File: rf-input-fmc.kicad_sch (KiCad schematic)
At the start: 0 parts

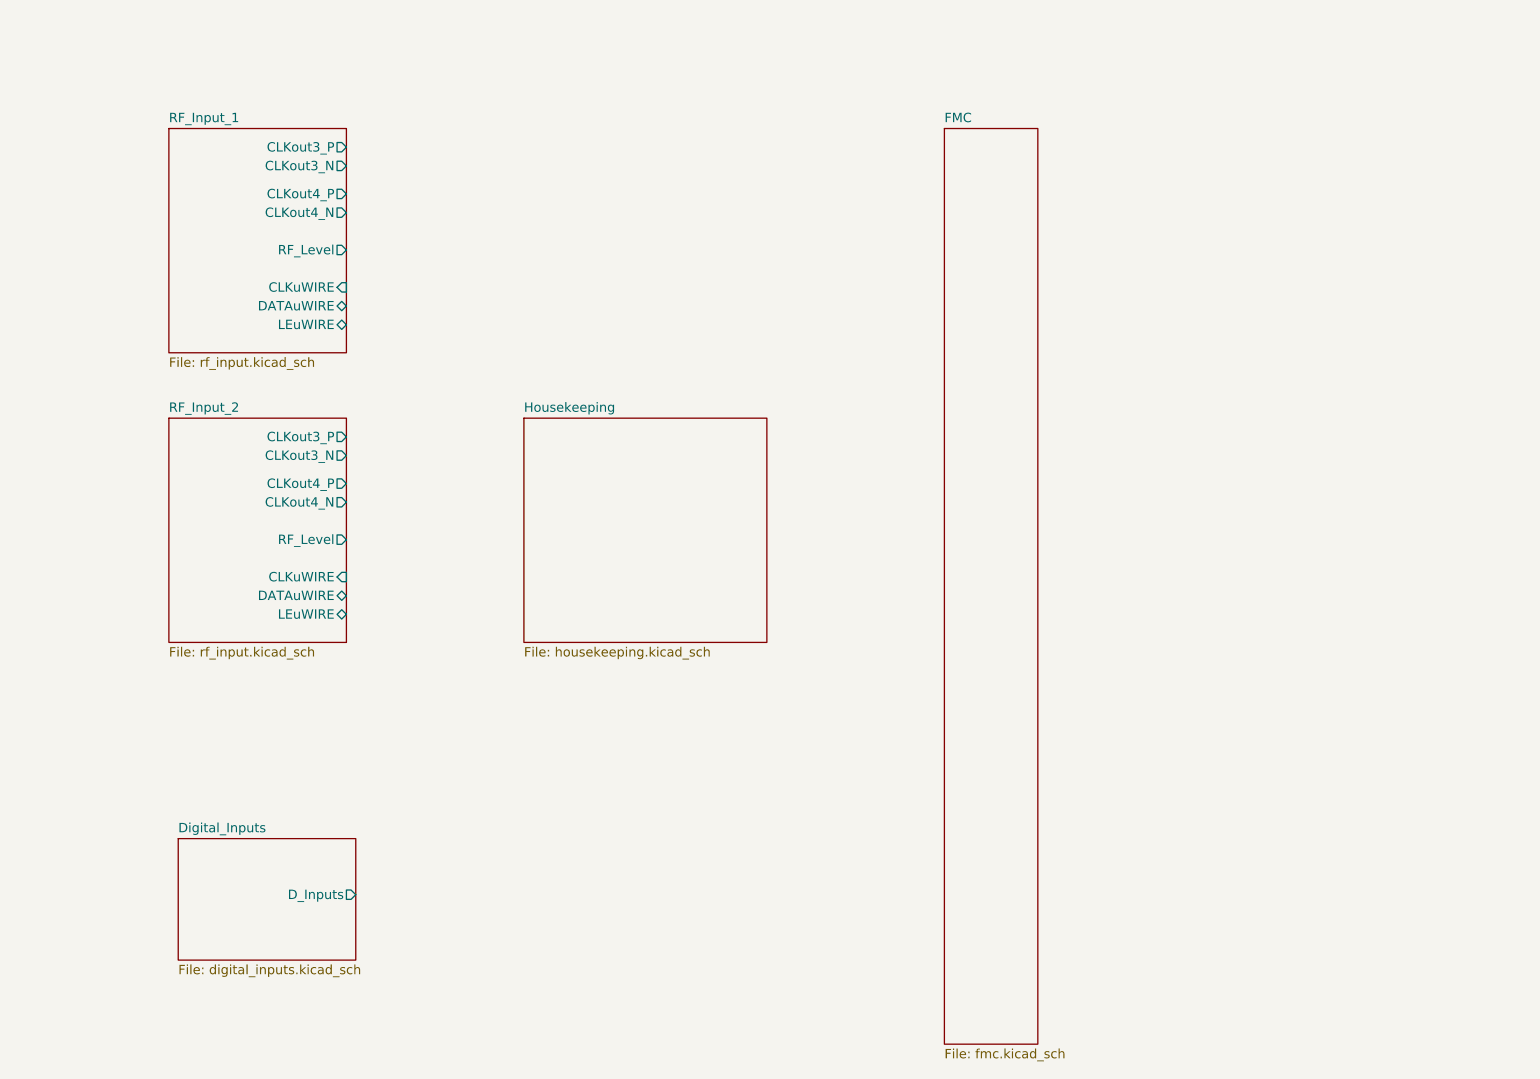
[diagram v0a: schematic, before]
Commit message: Draft Schematic Complete
-See design.md for remaining design work/questions
-See output folder for current schematic prints
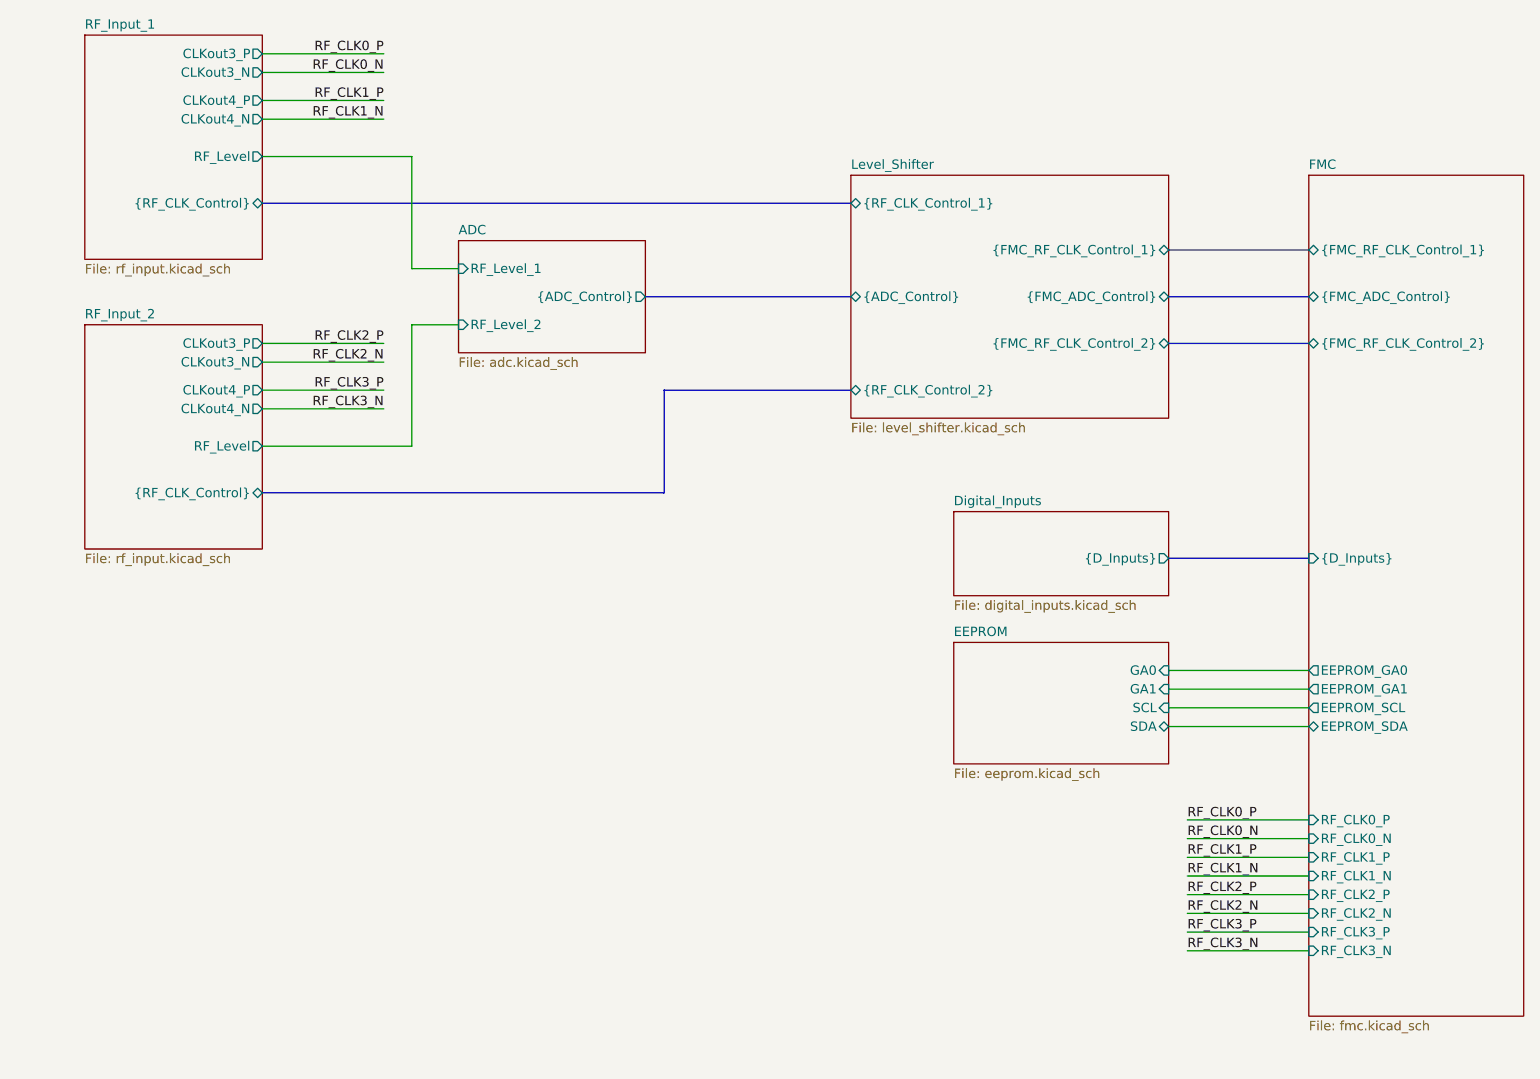
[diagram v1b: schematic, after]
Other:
- sheet Housekeeping renamed Level_Shifter
- added sheet ADC (adc.kicad_sch)
- added sheet EEPROM (eeprom.kicad_sch)
- sheet Digital_Inputs ports: added {D_Inputs}; removed D_Inputs
- sheet FMC ports: added EEPROM_GA0, EEPROM_GA1, EEPROM_SCL, EEPROM_SDA, RF_CLK0_N, RF_CLK0_P, RF_CLK1_N, RF_CLK1_P, RF_CLK2_N, RF_CLK2_P, RF_CLK3_N, RF_CLK3_P, {D_Inputs}, {FMC_ADC_Control}, {FMC_RF_CLK_Control_1}, {FMC_RF_CLK_Control_2}; removed none
- sheet Level_Shifter: file housekeeping.kicad_sch -> level_shifter.kicad_sch
- sheet Level_Shifter ports: added {ADC_Control}, {FMC_ADC_Control}, {FMC_RF_CLK_Control_1}, {FMC_RF_CLK_Control_2}, {RF_CLK_Control_1}, {RF_CLK_Control_2}; removed none
- sheet RF_Input_1 ports: added {RF_CLK_Control}; removed CLKuWIRE, DATAuWIRE, LEuWIRE
- sheet RF_Input_2 ports: added {RF_CLK_Control}; removed CLKuWIRE, DATAuWIRE, LEuWIRE
- company: (none) -> Osprey DCS
- title: (none) -> RF Input FMC Board

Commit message: fixup some hierarchical buses
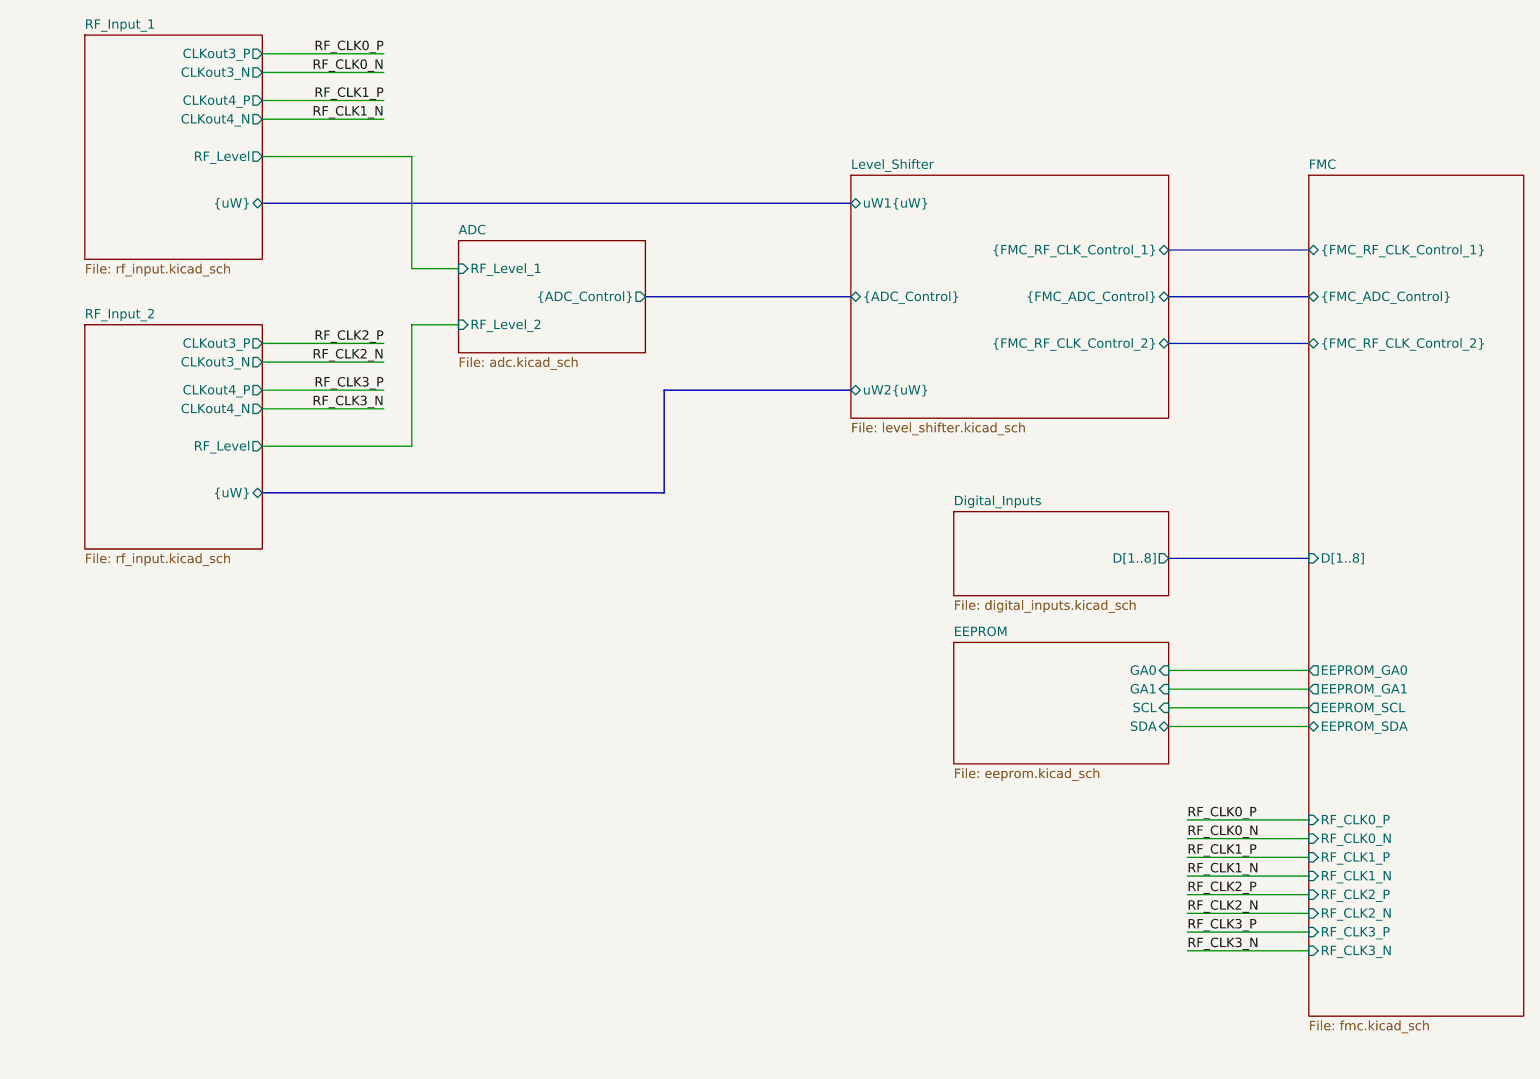
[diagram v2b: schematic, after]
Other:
- sheet Digital_Inputs ports: added D[1..8]; removed {D_Inputs}
- sheet FMC ports: added D[1..8]; removed {D_Inputs}
- sheet Level_Shifter ports: added uW1{uW}, uW2{uW}; removed {RF_CLK_Control_1}, {RF_CLK_Control_2}
- sheet RF_Input_1 ports: added {uW}; removed {RF_CLK_Control}
- sheet RF_Input_2 ports: added {uW}; removed {RF_CLK_Control}
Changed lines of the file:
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@@
 			)
 		)
-		(pin "{RF_CLK_Control}" bidirectional
+		(pin "{uW}" bidirectional
 			(at 69.85 86.36 0)
 			(effects
@@
 			)
 		)
-		(pin "{D_Inputs}" output
+		(pin "D[1..8]" output
 			(at 193.04 95.25 0)
 			(effects
@@
 			)
 		)
-		(pin "{RF_CLK_Control}" bidirectional
+		(pin "{uW}" bidirectional
 			(at 69.85 46.99 0)
 			(effects
@@
 			)
 		)
-		(pin "{RF_CLK_Control_1}" bidirectional
+		(pin "uW1{uW}" bidirectional
 			(at 149.86 46.99 180)
 			(effects
@@
 			)
 		)
-		(pin "{RF_CLK_Control_2}" bidirectional
+		(pin "uW2{uW}" bidirectional
 			(at 149.86 72.39 180)
 			(effects
@@
 			)
 		)
-		(pin "{D_Inputs}" input
+		(pin "D[1..8]" input
 			(at 212.09 95.25 180)
 			(effects

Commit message: Schamtic Revision
- Added 8 more D inputs
- Removed 1 LMK01801 IC
- Cleaned up some buses
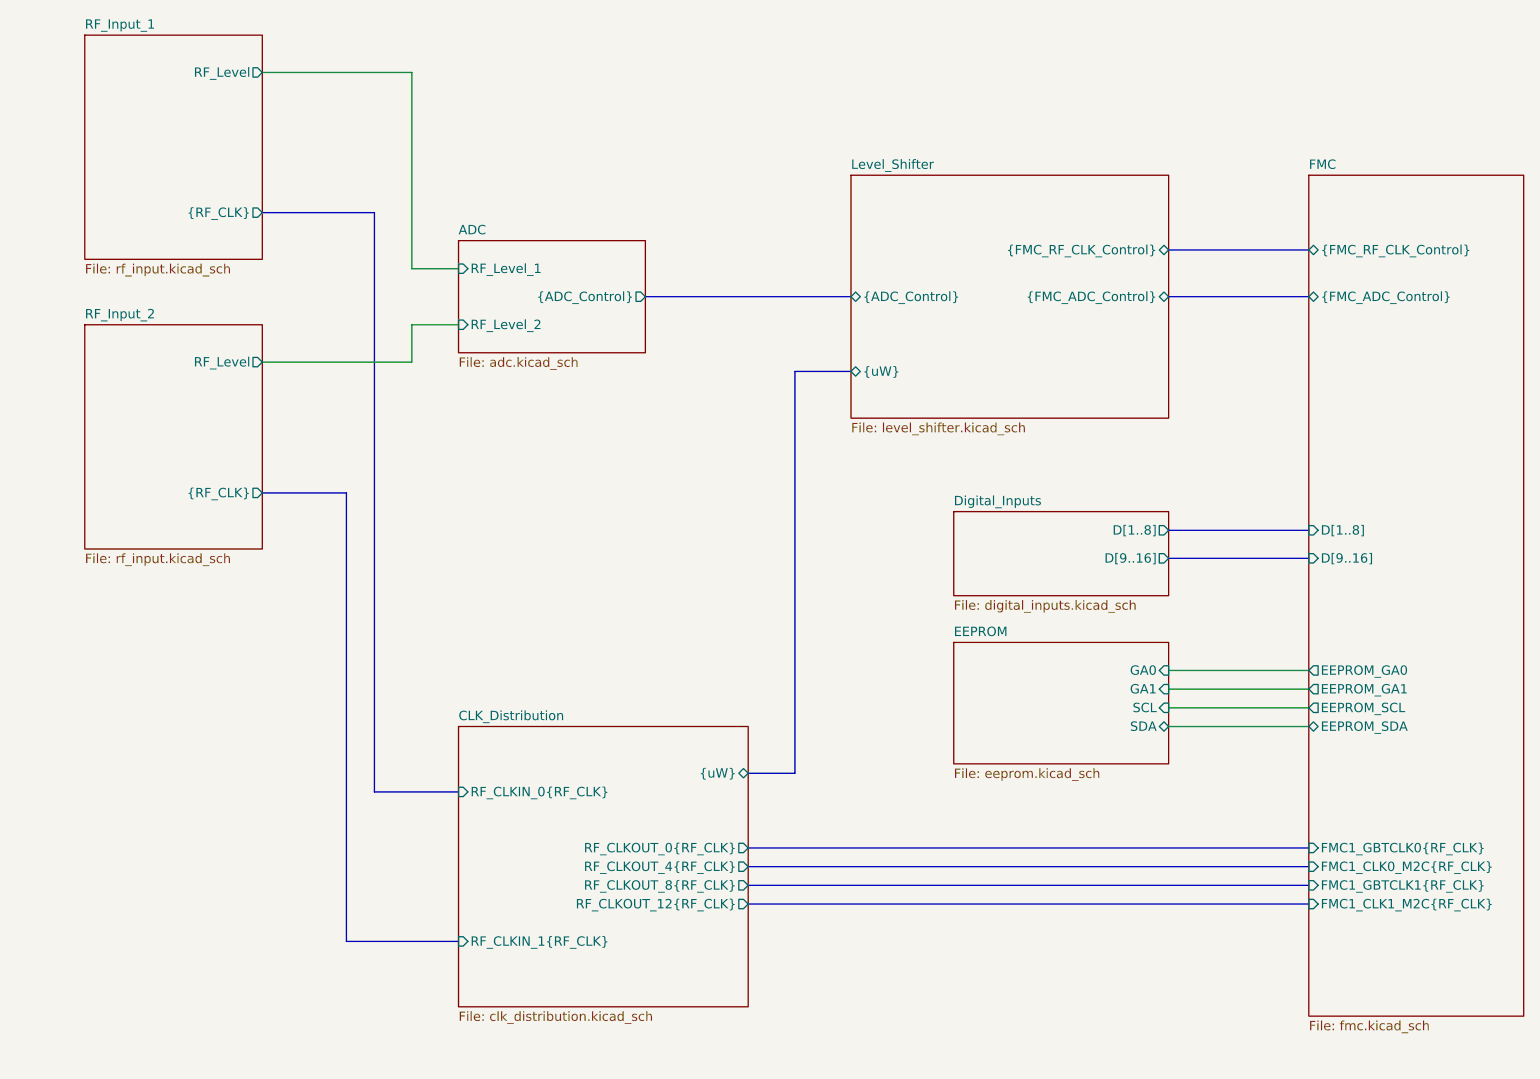
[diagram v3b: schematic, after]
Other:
- added sheet CLK_Distribution (clk_distribution.kicad_sch)
- sheet Digital_Inputs ports: added D[9..16]; removed none
- sheet FMC ports: added D[9..16], FMC1_CLK0_M2C{RF_CLK}, FMC1_CLK1_M2C{RF_CLK}, FMC1_GBTCLK0{RF_CLK}, FMC1_GBTCLK1{RF_CLK}, {FMC_RF_CLK_Control}; removed RF_CLK0_N, RF_CLK0_P, RF_CLK1_N, RF_CLK1_P, RF_CLK2_N, RF_CLK2_P, RF_CLK3_N, RF_CLK3_P, {FMC_RF_CLK_Control_1}, {FMC_RF_CLK_Control_2}
- sheet Level_Shifter ports: added {FMC_RF_CLK_Control}, {uW}; removed uW1{uW}, uW2{uW}, {FMC_RF_CLK_Control_1}, {FMC_RF_CLK_Control_2}
- sheet RF_Input_1 ports: added {RF_CLK}; removed CLKout3_N, CLKout3_P, CLKout4_N, CLKout4_P, {uW}
- sheet RF_Input_2 ports: added {RF_CLK}; removed CLKout3_N, CLKout3_P, CLKout4_N, CLKout4_P, {uW}

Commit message: Draft Schematic Revision
Schematic should be in good shape.
Meta-data and BOM need to be finished.
Very rough layout was started to floorplan out main parts and to see if we have room.
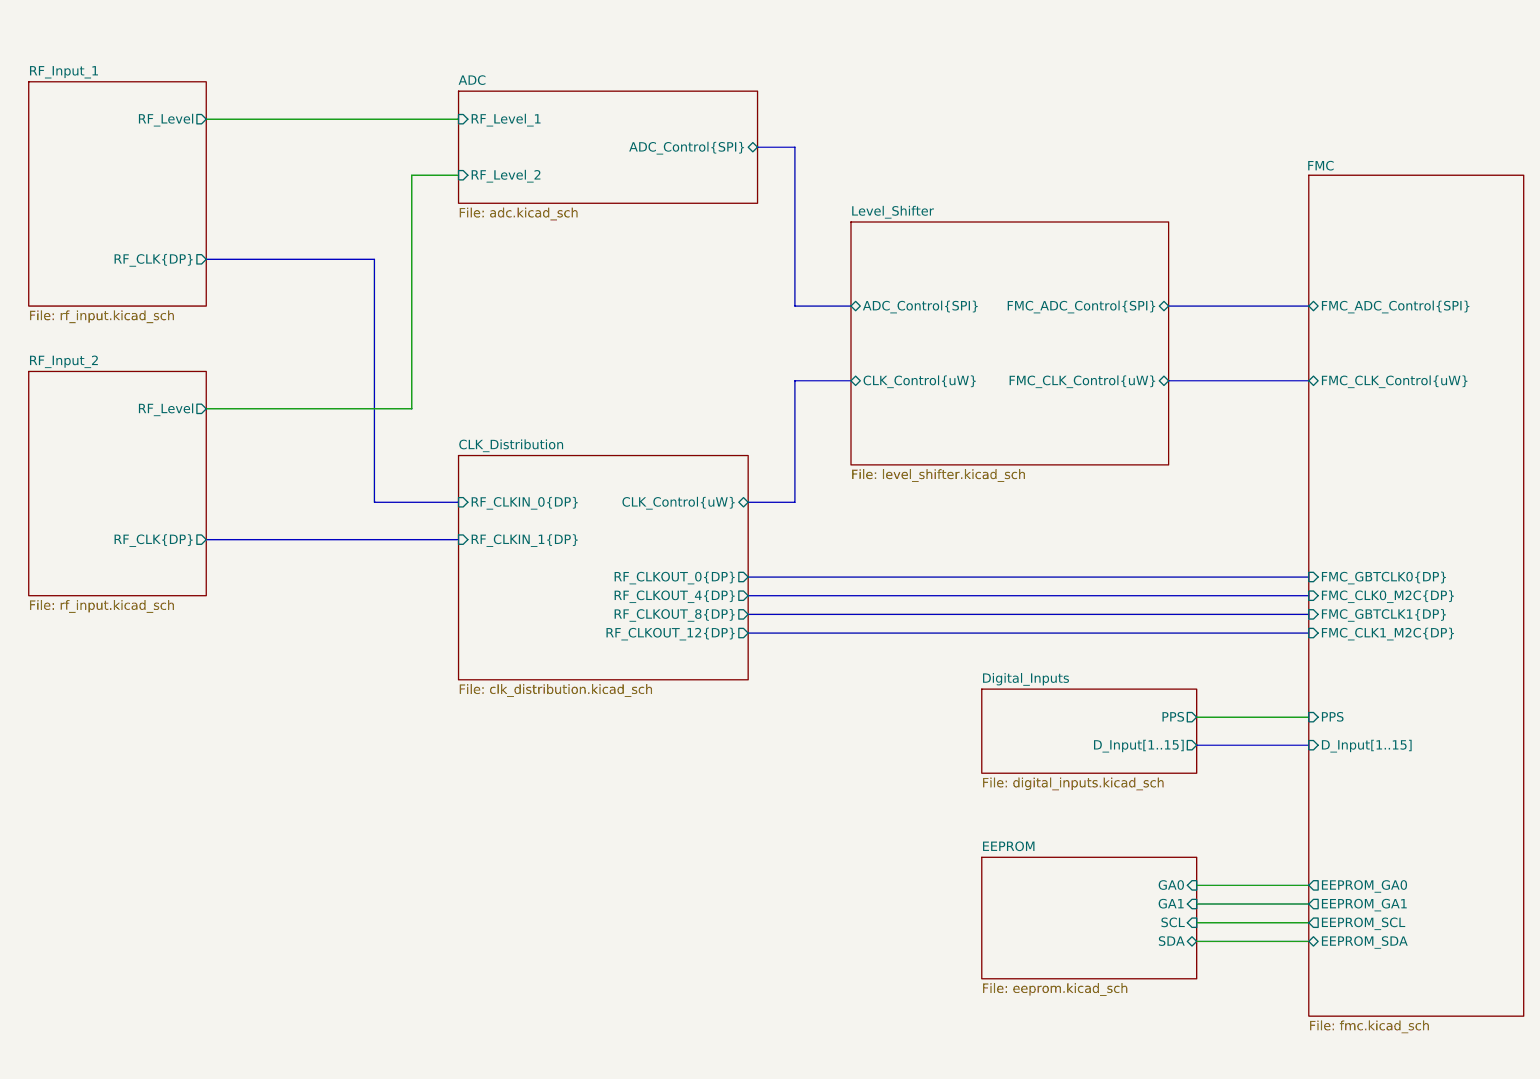
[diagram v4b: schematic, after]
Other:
- sheet ADC ports: added ADC_Control{SPI}; removed {ADC_Control}
- sheet CLK_Distribution ports: added CLK_Control{uW}, RF_CLKIN_0{DP}, RF_CLKIN_1{DP}, RF_CLKOUT_0{DP}, RF_CLKOUT_12{DP}, RF_CLKOUT_4{DP}, RF_CLKOUT_8{DP}; removed RF_CLKIN_0{RF_CLK}, RF_CLKIN_1{RF_CLK}, RF_CLKOUT_0{RF_CLK}, RF_CLKOUT_12{RF_CLK}, RF_CLKOUT_4{RF_CLK}, RF_CLKOUT_8{RF_CLK}, {uW}
- sheet Digital_Inputs ports: added D_Input[1..15], PPS; removed D[1..8], D[9..16]
- sheet FMC ports: added D_Input[1..15], FMC_ADC_Control{SPI}, FMC_CLK0_M2C{DP}, FMC_CLK1_M2C{DP}, FMC_CLK_Control{uW}, FMC_GBTCLK0{DP}, FMC_GBTCLK1{DP}, PPS; removed D[1..8], D[9..16], FMC1_CLK0_M2C{RF_CLK}, FMC1_CLK1_M2C{RF_CLK}, FMC1_GBTCLK0{RF_CLK}, FMC1_GBTCLK1{RF_CLK}, {FMC_ADC_Control}, {FMC_RF_CLK_Control}
- sheet Level_Shifter ports: added ADC_Control{SPI}, CLK_Control{uW}, FMC_ADC_Control{SPI}, FMC_CLK_Control{uW}; removed {ADC_Control}, {FMC_ADC_Control}, {FMC_RF_CLK_Control}, {uW}
- sheet RF_Input_1 ports: added RF_CLK{DP}; removed {RF_CLK}
- sheet RF_Input_2 ports: added RF_CLK{DP}; removed {RF_CLK}

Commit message: add copyright/license
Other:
- company: Osprey DCS -> SPDX-FileCopyrightText: 2025 Osprey DCS
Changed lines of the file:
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@@
 		(date "2025-10-01")
 		(rev "0.1")
-		(company "Osprey DCS")
-		(comment 1 "Pedro Rodriguez")
+		(company "SPDX-FileCopyrightText: 2025 Osprey DCS")
+		(comment 1 "SPDX-License-Identifier: CERN-OHL-S-2.0+")
 	)
 	(wire
